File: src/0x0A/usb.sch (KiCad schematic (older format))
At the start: 22 parts

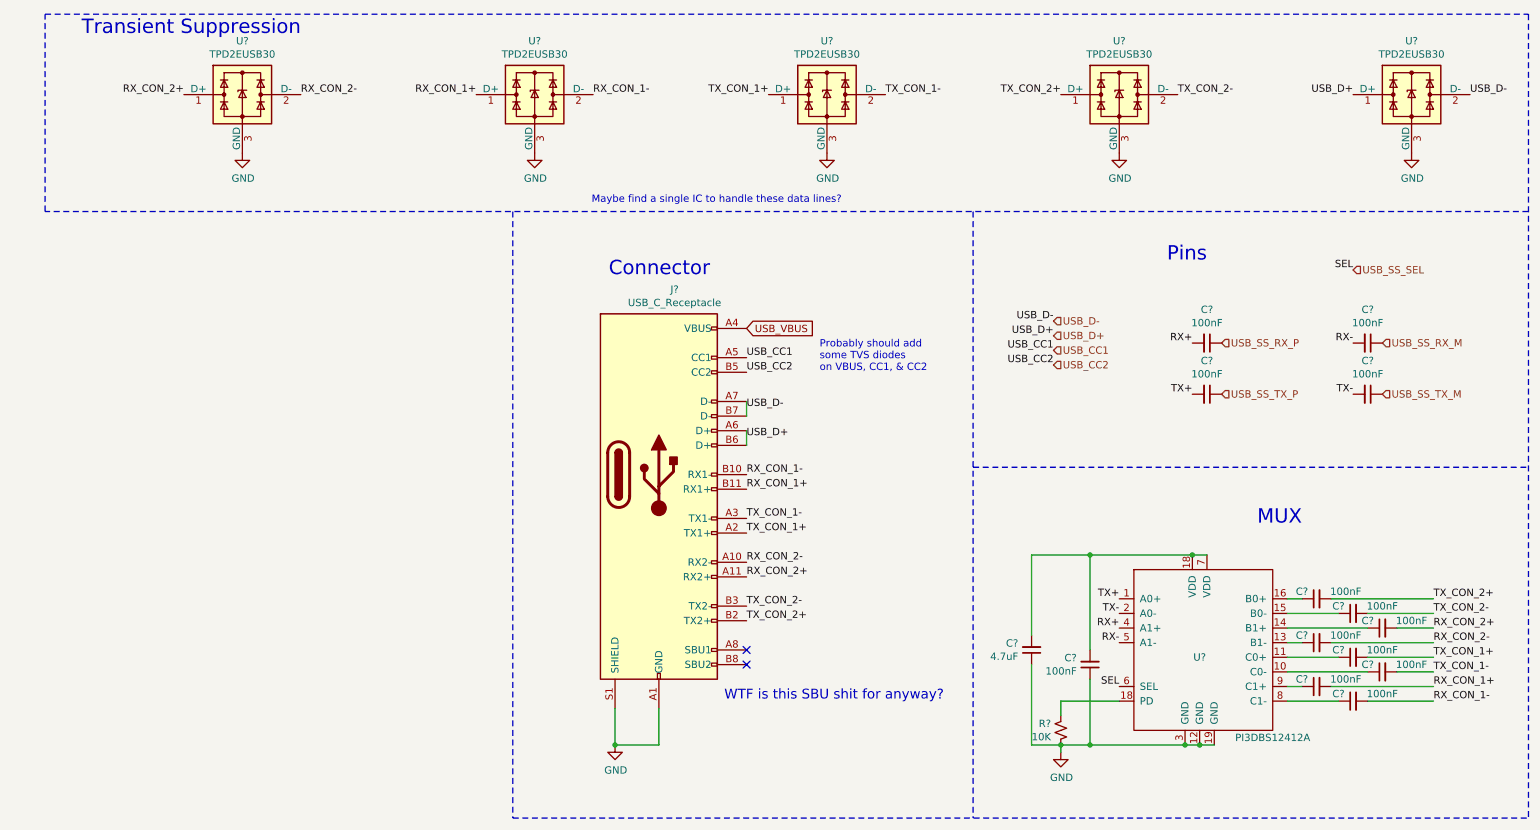
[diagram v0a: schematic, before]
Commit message: new file:   imgs/better.png 	modified:   src/0x0A/0x0A-cache.lib 	modified:   src/0x0A/0x0A.sch 	modified:   src/0x0A/antenna.sch 	modified:   src/0x0A/audio.sch 	modified:   src/0x0A/buttons.sch 	new file:   src/0x0A/cameras.sch 	modified:   src/0x0A/display.sch 	modified:   src/0x0A/gpio.sch 	modified:   src/0x0A/pwr.sch 	modified:   src/0x0A/sensors.sch 	modified:   src/0x0A/sim.sch 	modified:   src/0x0A/uart.sch 	modified:   src/0x0A/usb.sch 	new file:   src/models/body.obj 	new file:   src/models/phone.FCStd 	new file:   src/models/screen.obj
Added 3D models, integrated front & rear cameras, flash light, reformatting & more
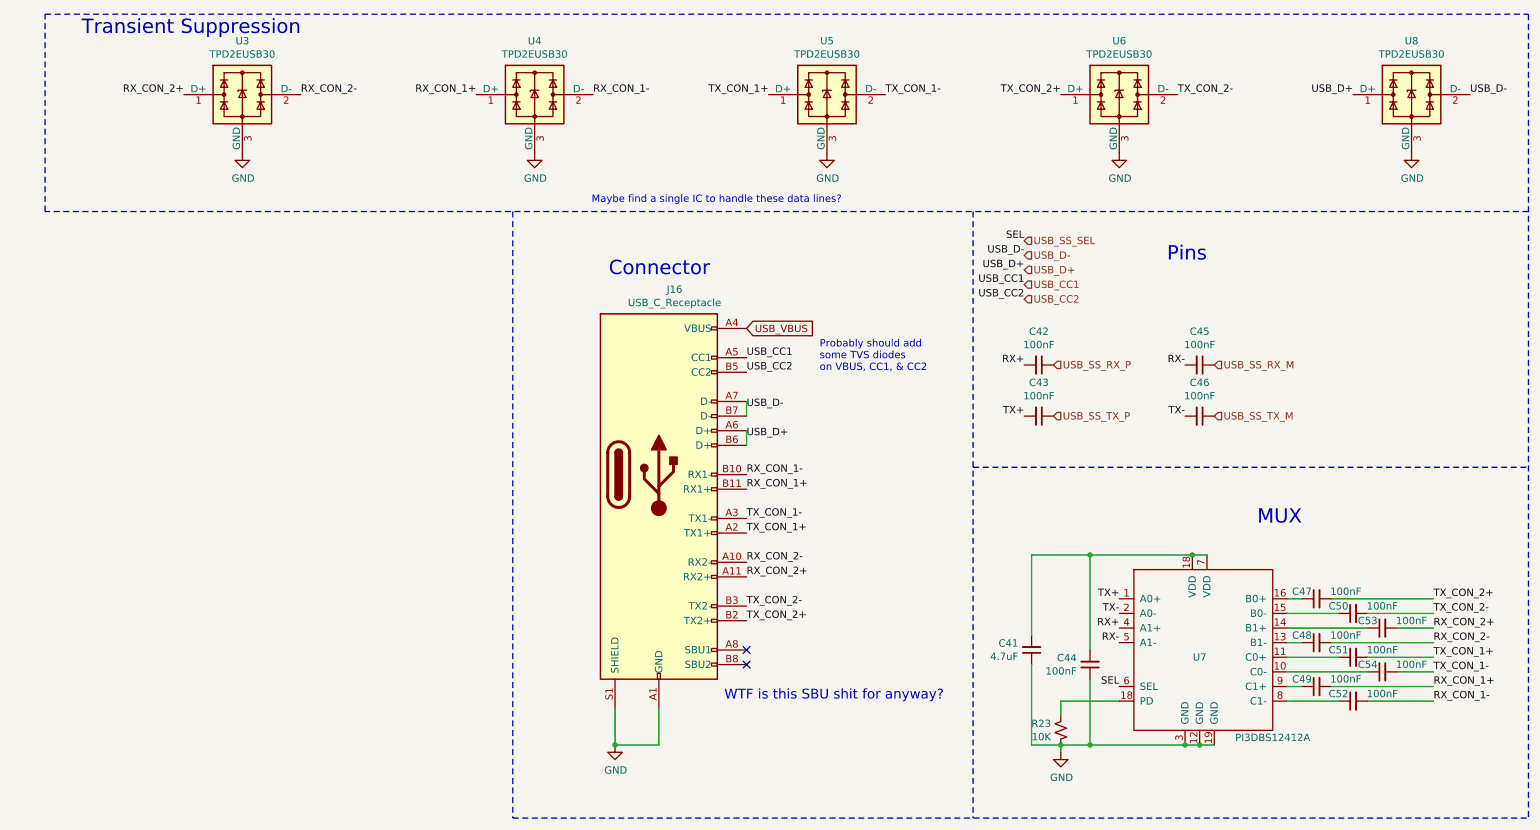
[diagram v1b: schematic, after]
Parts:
- C41, C42, C43, C44, C45, C46, C47, C48, C49, C50, C51, C52, C53, C54: renamed from C?; footprint (none) -> Capacitor_SMD:C_0603_1608Metric
- R23: renamed from R?; footprint (none) -> Resistor_SMD:R_0402_1005Metric
- gave numbers to parts that had none: 7
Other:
- moved on the sheet: C42, C43, C45, C46

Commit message: Updated schematics, started working on board layout
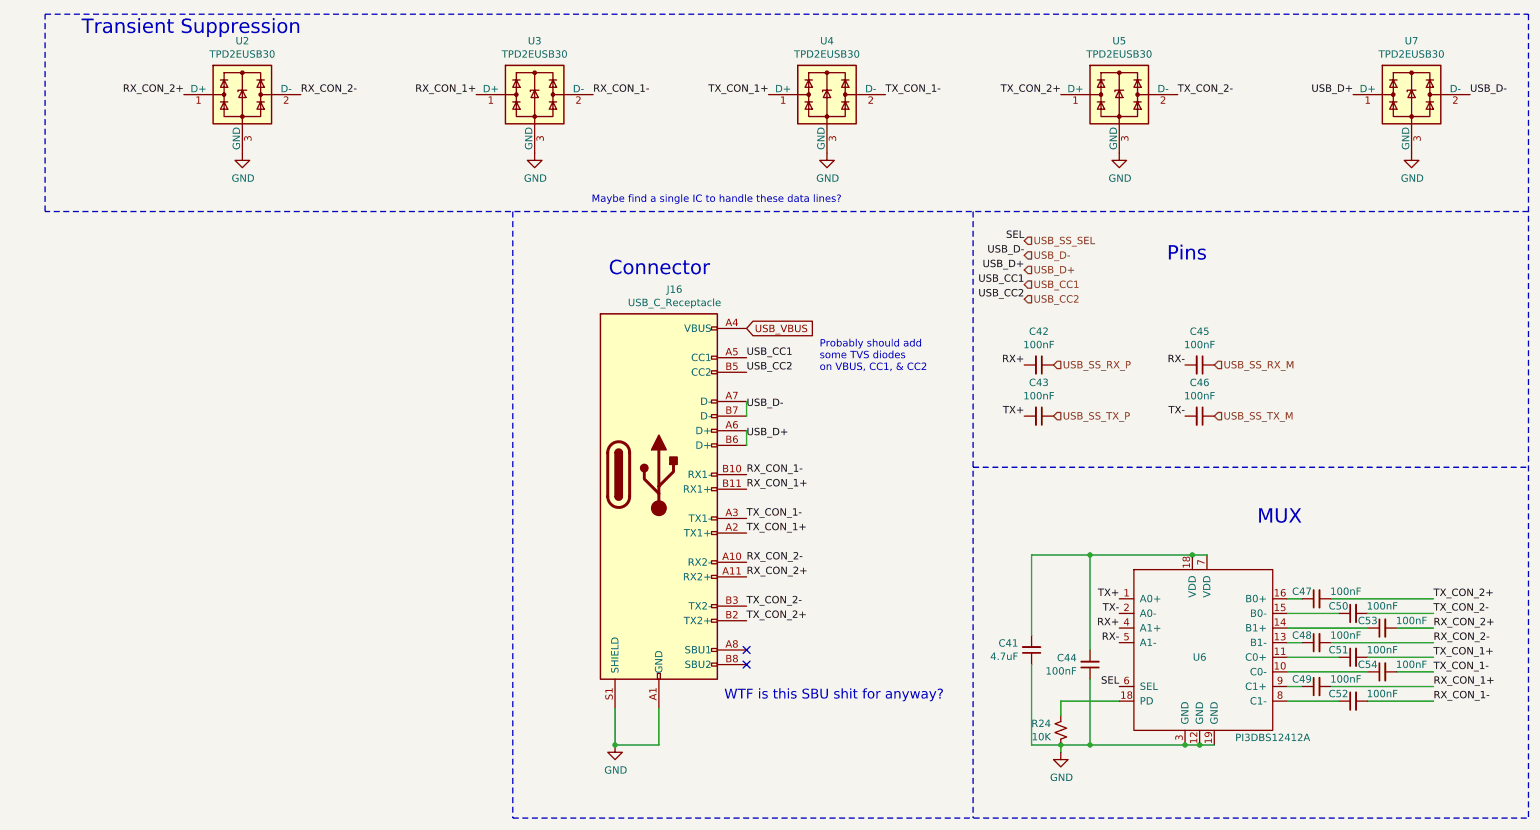
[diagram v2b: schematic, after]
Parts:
- C41: footprint Capacitor_SMD:C_0603_1608Metric -> Capacitor_SMD:C_0805_2012Metric; LCSC Part # (none) -> C1779
- C42, C43, C44, C45, C46, C47, C48, C49, C50, C51, C52, C53, C54: footprint Capacitor_SMD:C_0603_1608Metric -> Capacitor_SMD:C_0402_1005Metric; LCSC Part # (none) -> C307331
- J16: footprint (none) -> Connector_USB:USB_C_Receptacle_HRO_TYPE-C-31-M-12; LCSC Part # (none) -> C165948
- U6: renamed from U7; footprint (none) -> SnapEDA Library:CONV_MAX15035ETL+
- renumbered R23 to R24, U3 to U2, U4 to U3, U5 to U4, U6 to U5, U8 to U7
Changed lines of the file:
@@
 $Descr A4 11693 8268
 encoding utf-8
-Sheet 12 13
+Sheet 10 14
 Title "0x0A SmartPhone"
 Date "2022-09-01"
@@
 F 0 "J16" H 5207 5217 50  0000 C CNN
 F 1 "USB_C_Receptacle" H 5207 5126 50  0000 C CNN
-F 2 "" H 5250 3950 50  0001 C CNN
+F 2 "Connector_USB:USB_C_Receptacle_HRO_TYPE-C-31-M-12" H 5250 3950 50  0001 C CNN
 F 3 "https://www.usb.org/sites/default/files/documents/usb_type-c.zip" H 5250 3950 50  0001 C CNN
+F 4 "C165948" H 5100 3950 50  0001 C CNN "LCSC Part #"
 	1    5100 3950
 	1    0    0    -1
@@
 USB_SS_SEL
 $Comp
-L power:GND #PWR0161
+L power:GND #PWR065
 U 1 1 6427BF8E
 P 7850 5850
-F 0 "#PWR0161" H 7850 5600 50  0001 C CNN
+F 0 "#PWR065" H 7850 5600 50  0001 C CNN
 F 1 "GND" H 7855 5677 50  0000 C CNN
 F 2 "" H 7850 5850 50  0001 C CNN
@@
 $EndComp
 $Comp
-L Power_Protection:TPD2EUSB30 U4
+L Power_Protection:TPD2EUSB30 U3
 U 1 1 642BDD5E
 P 4250 1350
-F 0 "U4" H 4250 1717 50  0000 C CNN
+F 0 "U3" H 4250 1717 50  0000 C CNN
 F 1 "TPD2EUSB30" H 4250 1626 50  0000 C CNN
 F 2 "Package_TO_SOT_SMD:Texas_DRT-3" H 3500 1050 50  0001 C CNN
@@
 TX_CON_1-
 $Comp
-L Power_Protection:TPD2EUSB30 U5
+L Power_Protection:TPD2EUSB30 U4
 U 1 1 642DBDB1
 P 6250 1350
-F 0 "U5" H 6250 1717 50  0000 C CNN
+F 0 "U4" H 6250 1717 50  0000 C CNN
 F 1 "TPD2EUSB30" H 6250 1626 50  0000 C CNN
 F 2 "Package_TO_SOT_SMD:Texas_DRT-3" H 5500 1050 50  0001 C CNN
@@
 $EndComp
 $Comp
-L Power_Protection:TPD2EUSB30 U3
+L Power_Protection:TPD2EUSB30 U2
 U 1 1 642EFB0B
 P 2250 1350
-F 0 "U3" H 2250 1717 50  0000 C CNN
+F 0 "U2" H 2250 1717 50  0000 C CNN
 F 1 "TPD2EUSB30" H 2250 1626 50  0000 C CNN
 F 2 "Package_TO_SOT_SMD:Texas_DRT-3" H 1500 1050 50  0001 C CNN
@@
 RX_CON_2+
 $Comp
-L Power_Protection:TPD2EUSB30 U6
+L Power_Protection:TPD2EUSB30 U5
 U 1 1 642F3F30
 P 8250 1350
-F 0 "U6" H 8250 1717 50  0000 C CNN
+F 0 "U5" H 8250 1717 50  0000 C CNN
 F 1 "TPD2EUSB30" H 8250 1626 50  0000 C CNN
 F 2 "Package_TO_SOT_SMD:Texas_DRT-3" H 7500 1050 50  0001 C CNN
@@
 TX_CON_2-
 $Comp
-L power:GND #PWR0162
+L power:GND #PWR061
 U 1 1 64339716
 P 2250 1750
-F 0 "#PWR0162" H 2250 1500 50  0001 C CNN
+F 0 "#PWR061" H 2250 1500 50  0001 C CNN
 F 1 "GND" H 2255 1577 50  0000 C CNN
 F 2 "" H 2250 1750 50  0001 C CNN
@@
 $EndComp
 $Comp
-L power:GND #PWR0163
+L power:GND #PWR062
 U 1 1 6433987A
 P 4250 1750
-F 0 "#PWR0163" H 4250 1500 50  0001 C CNN
+F 0 "#PWR062" H 4250 1500 50  0001 C CNN
 F 1 "GND" H 4255 1577 50  0000 C CNN
 F 2 "" H 4250 1750 50  0001 C CNN
@@
 $EndComp
 $Comp
-L power:GND #PWR0164
+L power:GND #PWR064
 U 1 1 64339A56
 P 6250 1750
-F 0 "#PWR0164" H 6250 1500 50  0001 C CNN
+F 0 "#PWR064" H 6250 1500 50  0001 C CNN
 F 1 "GND" H 6255 1577 50  0000 C CNN
 F 2 "" H 6250 1750 50  0001 C CNN
@@
 $EndComp
 $Comp
-L power:GND #PWR0165
+L power:GND #PWR066
 U 1 1 6433A022
 P 8250 1750
-F 0 "#PWR0165" H 8250 1500 50  0001 C CNN
+F 0 "#PWR066" H 8250 1500 50  0001 C CNN
 F 1 "GND" H 8255 1577 50  0000 C CNN
 F 2 "" H 8250 1750 50  0001 C CNN
@@
 $EndComp
 $Comp
-L Power_Protection:TPD2EUSB30 U8
+L Power_Protection:TPD2EUSB30 U7
 U 1 1 64342971
 P 10250 1350
-F 0 "U8" H 10250 1717 50  0000 C CNN
+F 0 "U7" H 10250 1717 50  0000 C CNN
 F 1 "TPD2EUSB30" H 10250 1626 50  0000 C CNN
 F 2 "Package_TO_SOT_SMD:Texas_DRT-3" H 9500 1050 50  0001 C CNN
@@
 USB_D+
 $Comp
-L power:GND #PWR0166
+L power:GND #PWR067
 U 1 1 6435911E
 P 10250 1750
-F 0 "#PWR0166" H 10250 1500 50  0001 C CNN
+F 0 "#PWR067" H 10250 1500 50  0001 C CNN
 F 1 "GND" H 10255 1577 50  0000 C CNN
 F 2 "" H 10250 1750 50  0001 C CNN
@@
 	5700 3750 5700 3650
 $Comp
-L custom:PI3DBS12412A U7
+L custom:PI3DBS12412A U6
 U 1 1 6442DDFA
 P 8800 4350
-F 0 "U7" H 8800 3500 50  0000 C CNN
+F 0 "U6" H 8800 3500 50  0000 C CNN
 F 1 "PI3DBS12412A" H 9300 2950 50  0000 C CNN
-F 2 "" H 8800 4350 50  0001 C CNN
+F 2 "SnapEDA Library:CONV_MAX15035ETL+" H 8800 4350 50  0001 C CNN
 F 3 "" H 8800 4350 50  0001 C CNN
 	1    8800 4350
@@
 SEL
 $Comp
-L Device:R_Small_US R23
+L Device:R_Small_US R24
 U 1 1 6443DD93
 P 7850 5700
-F 0 "R23" H 7783 5654 50  0000 R CNN
+F 0 "R24" H 7783 5654 50  0000 R CNN
 F 1 "10K" H 7783 5745 50  0000 R CNN
 F 2 "Resistor_SMD:R_0402_1005Metric" H 7850 5700 50  0001 C CNN
@@
 F 0 "C41" H 7559 5104 50  0000 R CNN
 F 1 "4.7uF" H 7559 5195 50  0000 R CNN
-F 2 "Capacitor_SMD:C_0603_1608Metric" H 7650 5150 50  0001 C CNN
+F 2 "Capacitor_SMD:C_0805_2012Metric" H 7650 5150 50  0001 C CNN
 F 3 "~" H 7650 5150 50  0001 C CNN
+F 4 "C1779" H 7650 5150 50  0001 C CNN "LCSC Part #"
 	1    7650 5150
 	1    0    0    1
@@
 F 0 "C44" H 7959 5204 50  0000 R CNN
 F 1 "100nF" H 7959 5295 50  0000 R CNN
-F 2 "Capacitor_SMD:C_0603_1608Metric" H 8050 5250 50  0001 C CNN
+F 2 "Capacitor_SMD:C_0402_1005Metric" H 8050 5250 50  0001 C CNN
 F 3 "~" H 8050 5250 50  0001 C CNN
+F 4 "C307331" H 8050 5250 50  0001 C CNN "LCSC Part #"
 	1    8050 5250
 	1    0    0    1
@@
 F 0 "C47" V 9550 4900 50  0000 C CNN
 F 1 "100nF" V 9550 4600 50  0000 C CNN
-F 2 "Capacitor_SMD:C_0603_1608Metric" H 9600 4800 50  0001 C CNN
+F 2 "Capacitor_SMD:C_0402_1005Metric" H 9600 4800 50  0001 C CNN
 F 3 "~" H 9600 4800 50  0001 C CNN
+F 4 "C307331" H 9600 4800 50  0001 C CNN "LCSC Part #"
 	1    9600 4800
 	0    -1   1    0
@@
 F 0 "C50" V 9800 5000 50  0000 C CNN
 F 1 "100nF" V 9800 4700 50  0000 C CNN
-F 2 "Capacitor_SMD:C_0603_1608Metric" H 9850 4900 50  0001 C CNN
+F 2 "Capacitor_SMD:C_0402_1005Metric" H 9850 4900 50  0001 C CNN
 F 3 "~" H 9850 4900 50  0001 C CNN
+F 4 "C307331" H 9850 4900 50  0001 C CNN "LCSC Part #"
 	1    9850 4900
 	0    -1   1    0
@@
 F 0 "C53" V 10000 5100 50  0000 C CNN
 F 1 "100nF" V 10000 4800 50  0000 C CNN
-F 2 "Capacitor_SMD:C_0603_1608Metric" H 10050 5000 50  0001 C CNN
+F 2 "Capacitor_SMD:C_0402_1005Metric" H 10050 5000 50  0001 C CNN
 F 3 "~" H 10050 5000 50  0001 C CNN
+F 4 "C307331" H 10050 5000 50  0001 C CNN "LCSC Part #"
 	1    10050 5000
 	0    -1   1    0
@@
 F 0 "C48" V 9550 5200 50  0000 C CNN
 F 1 "100nF" V 9550 4900 50  0000 C CNN
-F 2 "Capacitor_SMD:C_0603_1608Metric" H 9600 5100 50  0001 C CNN
+F 2 "Capacitor_SMD:C_0402_1005Metric" H 9600 5100 50  0001 C CNN
 F 3 "~" H 9600 5100 50  0001 C CNN
+F 4 "C307331" H 9600 5100 50  0001 C CNN "LCSC Part #"
 	1    9600 5100
 	0    -1   1    0
@@
 F 0 "C51" V 9800 5300 50  0000 C CNN
 F 1 "100nF" V 9800 5000 50  0000 C CNN
-F 2 "Capacitor_SMD:C_0603_1608Metric" H 9850 5200 50  0001 C CNN
+F 2 "Capacitor_SMD:C_0402_1005Metric" H 9850 5200 50  0001 C CNN
 F 3 "~" H 9850 5200 50  0001 C CNN
+F 4 "C307331" H 9850 5200 50  0001 C CNN "LCSC Part #"
 	1    9850 5200
 	0    -1   1    0
@@
 F 0 "C54" V 10000 5400 50  0000 C CNN
 F 1 "100nF" V 10000 5100 50  0000 C CNN
-F 2 "Capacitor_SMD:C_0603_1608Metric" H 10050 5300 50  0001 C CNN
+F 2 "Capacitor_SMD:C_0402_1005Metric" H 10050 5300 50  0001 C CNN
 F 3 "~" H 10050 5300 50  0001 C CNN
+F 4 "C307331" H 10050 5300 50  0001 C CNN "LCSC Part #"
 	1    10050 5300
 	0    -1   1    0
@@
 F 0 "C49" V 9550 5500 50  0000 C CNN
 F 1 "100nF" V 9550 5200 50  0000 C CNN
-F 2 "Capacitor_SMD:C_0603_1608Metric" H 9600 5400 50  0001 C CNN
+F 2 "Capacitor_SMD:C_0402_1005Metric" H 9600 5400 50  0001 C CNN
 F 3 "~" H 9600 5400 50  0001 C CNN
+F 4 "C307331" H 9600 5400 50  0001 C CNN "LCSC Part #"
 	1    9600 5400
 	0    -1   1    0
@@
 F 0 "C52" V 9800 5600 50  0000 C CNN
 F 1 "100nF" V 9800 5300 50  0000 C CNN
-F 2 "Capacitor_SMD:C_0603_1608Metric" H 9850 5500 50  0001 C CNN
+F 2 "Capacitor_SMD:C_0402_1005Metric" H 9850 5500 50  0001 C CNN
 F 3 "~" H 9850 5500 50  0001 C CNN
+F 4 "C307331" H 9850 5500 50  0001 C CNN "LCSC Part #"
 	1    9850 5500
 	0    -1   1    0
@@
 F 0 "C42" V 7471 3200 50  0000 C CNN
 F 1 "100nF" V 7562 3200 50  0000 C CNN
-F 2 "Capacitor_SMD:C_0603_1608Metric" H 7700 3200 50  0001 C CNN
+F 2 "Capacitor_SMD:C_0402_1005Metric" H 7700 3200 50  0001 C CNN
 F 3 "~" H 7700 3200 50  0001 C CNN
+F 4 "C307331" H 7700 3200 50  0001 C CNN "LCSC Part #"
 	1    7700 3200
 	0    1    1    0
@@
 F 0 "C45" V 8571 3200 50  0000 C CNN
 F 1 "100nF" V 8662 3200 50  0000 C CNN
-F 2 "Capacitor_SMD:C_0603_1608Metric" H 8800 3200 50  0001 C CNN
+F 2 "Capacitor_SMD:C_0402_1005Metric" H 8800 3200 50  0001 C CNN
 F 3 "~" H 8800 3200 50  0001 C CNN
+F 4 "C307331" H 8800 3200 50  0001 C CNN "LCSC Part #"
 	1    8800 3200
 	0    1    1    0
@@
 F 0 "C43" V 7471 3550 50  0000 C CNN
 F 1 "100nF" V 7562 3550 50  0000 C CNN
-F 2 "Capacitor_SMD:C_0603_1608Metric" H 7700 3550 50  0001 C CNN
+F 2 "Capacitor_SMD:C_0402_1005Metric" H 7700 3550 50  0001 C CNN
 F 3 "~" H 7700 3550 50  0001 C CNN
+F 4 "C307331" H 7700 3550 50  0001 C CNN "LCSC Part #"
 	1    7700 3550
 	0    1    1    0
@@
 F 0 "C46" V 8571 3550 50  0000 C CNN
 F 1 "100nF" V 8662 3550 50  0000 C CNN
-F 2 "Capacitor_SMD:C_0603_1608Metric" H 8800 3550 50  0001 C CNN
+F 2 "Capacitor_SMD:C_0402_1005Metric" H 8800 3550 50  0001 C CNN
 F 3 "~" H 8800 3550 50  0001 C CNN
+F 4 "C307331" H 8800 3550 50  0001 C CNN "LCSC Part #"
 	1    8800 3550
 	0    1    1    0
@@
 NoConn ~ 5700 5250
 $Comp
-L power:GND #PWR0167
+L power:GND #PWR063
 U 1 1 649865E4
 P 4800 5800
-F 0 "#PWR0167" H 4800 5550 50  0001 C CNN
+F 0 "#PWR063" H 4800 5550 50  0001 C CNN
 F 1 "GND" H 4805 5627 50  0000 C CNN
 F 2 "" H 4800 5800 50  0001 C CNN
